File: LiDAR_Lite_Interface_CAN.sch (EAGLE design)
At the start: 30 parts, among them J1 CONN_6SCREW_2.54, J2 CONN_42.54_SCREW, Q1 2N7002, Q2 2N7002, Q3 DMG3404, Q4 MOSFET_PCH-NX2301P, U1 TLV61220DBV, U2 TS5A23157DGS

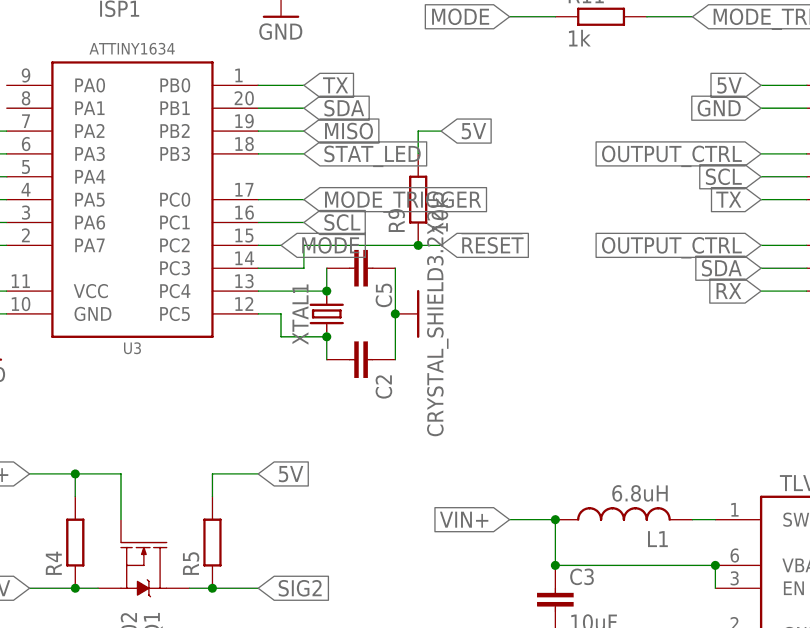
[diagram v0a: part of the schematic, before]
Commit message: Updated layout, added variants
Improved layout, potentially add button, then ready to send to fab. Added variations of layout for potential future alteration
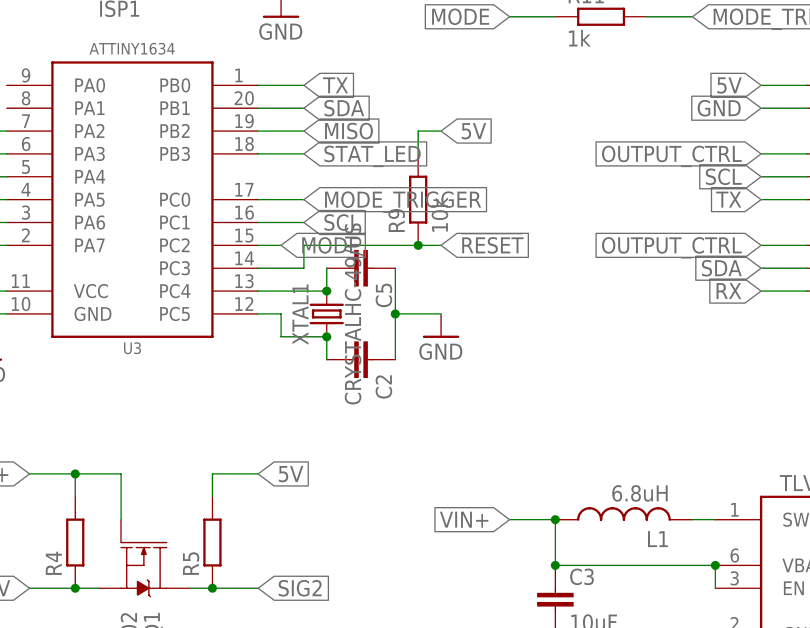
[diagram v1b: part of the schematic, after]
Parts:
- XTAL1: value CRYSTAL_SHIELD3.2X2.5 -> CRYSTALHC-49/US; device bschulz:CRYSTAL_SHIELD3.2X2.5 -> bschulz:CRYSTALHC-49/US; DIGIKEY 535-10901-1-ND -> (none); MF Abricon -> (none); MPN ABM8G-12.000MHZ-4Y-T3 -> (none)
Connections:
- net GND: no longer XTAL1.GND
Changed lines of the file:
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@@
 <part name="GND5" library="supply1" library_urn="urn:adsk.eagle:library:371" deviceset="GND" device=""/>
 <part name="Q4" library="bschulz" deviceset="MOSFET_PCH" device="-NX2301P"/>
-<part name="XTAL1" library="bschulz" deviceset="CRYSTAL_SHIELD" device="3.2X2.5">
-<attribute name="DIGIKEY" value="535-10901-1-ND"/>
-<attribute name="MF" value="Abricon"/>
-<attribute name="MPN" value="ABM8G-12.000MHZ-4Y-T3"/>
-</part>
 <part name="C2" library="bschulz_passives" deviceset="C-EU" device="C0603" technology="10PF"/>
 <part name="C5" library="bschulz_passives" deviceset="C-EU" device="C0603" technology="10PF"/>
@@
 <part name="R11" library="bschulz_passives" deviceset="R-EU_" device="R0603" technology="1K" value="1k"/>
 <part name="U2" library="bschulz" deviceset="TS5A23157" device="DGS"/>
+<part name="XTAL1" library="bschulz" deviceset="CRYSTAL" device="HC-49/US"/>
+<part name="GND7" library="supply1" library_urn="urn:adsk.eagle:library:371" deviceset="GND" device=""/>
 </parts>
 <sheets>
@@
 <attribute name="VALUE" x="165.1" y="2.54" size="1.778" layer="96" font="vector" rot="R270"/>
 </instance>
-<instance part="XTAL1" gate="G$1" x="86.36" y="66.04" smashed="yes" rot="R90">
-<attribute name="NAME" x="84.328" y="66.04" size="1.778" layer="95" font="vector" rot="R90" align="bottom-center"/>
-<attribute name="VALUE" x="97.536" y="66.04" size="1.778" layer="96" font="vector" rot="R90" align="top-center"/>
-<attribute name="MF" x="86.36" y="66.04" size="1.778" layer="96" rot="R90" display="off"/>
-<attribute name="MPN" x="86.36" y="66.04" size="1.778" layer="96" rot="R90" display="off"/>
-<attribute name="DIGIKEY" x="86.36" y="66.04" size="1.778" layer="96" rot="R90" display="off"/>
-</instance>
 <instance part="C2" gate="G$1" x="91.44" y="60.96" smashed="yes" rot="R270">
 <attribute name="NAME" x="91.821" y="59.436" size="1.778" layer="95" rot="R270"/>
@@
 <attribute name="DISP" x="152.4" y="95.758" size="1.778" layer="95" ratio="15" align="center"/>
 <attribute name="NAME" x="152.4" y="64.008" size="1.778" layer="95" ratio="15" align="center"/>
+</instance>
+<instance part="XTAL1" gate="G$1" x="86.36" y="66.04" smashed="yes" rot="R90">
+<attribute name="NAME" x="84.328" y="66.04" size="1.778" layer="95" font="vector" rot="R90" align="bottom-center"/>
+<attribute name="VALUE" x="88.392" y="66.04" size="1.778" layer="96" font="vector" rot="R90" align="top-center"/>
+</instance>
+<instance part="GND7" gate="1" x="99.06" y="63.5" smashed="yes">
+<attribute name="VALUE" x="96.52" y="60.96" size="1.778" layer="96"/>
 </instance>
 </instances>
@@
 </segment>
 <segment>
+<pinref part="C2" gate="G$1" pin="1"/>
 <pinref part="C5" gate="G$1" pin="1"/>
-<pinref part="XTAL1" gate="G$1" pin="GND"/>
 <wire x1="93.98" y1="71.12" x2="93.98" y2="66.04" width="0.1524" layer="91"/>
-<pinref part="C2" gate="G$1" pin="1"/>
-<wire x1="93.98" y1="60.96" x2="93.98" y2="66.04" width="0.1524" layer="91"/>
+<pinref part="GND7" gate="1" pin="GND"/>
+<wire x1="93.98" y1="66.04" x2="93.98" y2="60.96" width="0.1524" layer="91"/>
+<wire x1="93.98" y1="66.04" x2="99.06" y2="66.04" width="0.1524" layer="91"/>
 <junction x="93.98" y="66.04"/>
 </segment>
@@
 <net name="N$1" class="0">
 <segment>
-<pinref part="XTAL1" gate="G$1" pin="2"/>
 <pinref part="C5" gate="G$1" pin="2"/>
 <wire x1="86.36" y1="68.58" x2="86.36" y2="71.12" width="0.1524" layer="91"/>
 <pinref part="U3" gate="G$1" pin="PC4"/>
 <wire x1="86.36" y1="68.58" x2="78.74" y2="68.58" width="0.1524" layer="91"/>
+<pinref part="XTAL1" gate="G$1" pin="2"/>
 <junction x="86.36" y="68.58"/>
 </segment>
@@
 <segment>
 <pinref part="C2" gate="G$1" pin="2"/>
-<pinref part="XTAL1" gate="G$1" pin="1"/>
 <wire x1="86.36" y1="60.96" x2="86.36" y2="63.5" width="0.1524" layer="91"/>
 <wire x1="86.36" y1="63.5" x2="81.28" y2="63.5" width="0.1524" layer="91"/>
-<junction x="86.36" y="63.5"/>
 <wire x1="81.28" y1="63.5" x2="81.28" y2="66.04" width="0.1524" layer="91"/>
 <pinref part="U3" gate="G$1" pin="PC5"/>
 <wire x1="81.28" y1="66.04" x2="78.74" y2="66.04" width="0.1524" layer="91"/>
-</segment>
-</net>
+<pinref part="XTAL1" gate="G$1" pin="1"/>
+<junction x="86.36" y="63.5"/>
+</segment>
+</net>
